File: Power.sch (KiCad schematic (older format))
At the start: 27 parts, among them J16 +15V, J17 GND, J18 WE 691216710002, J19 Conn_02x04_Counter_Clockwise, J20 Conn_02x04_Counter_Clockwise, J21 Conn_02x04_Counter_Clockwise, U8 AMS1117-3.3, U9 AMS1117-3.3

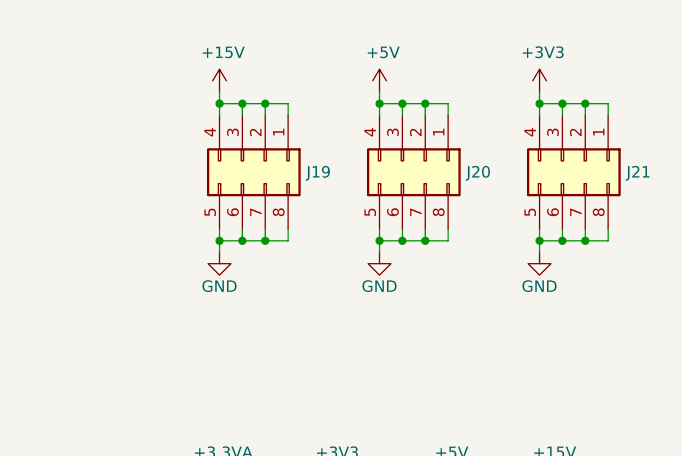
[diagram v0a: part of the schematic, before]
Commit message: MCU prepped for fanout
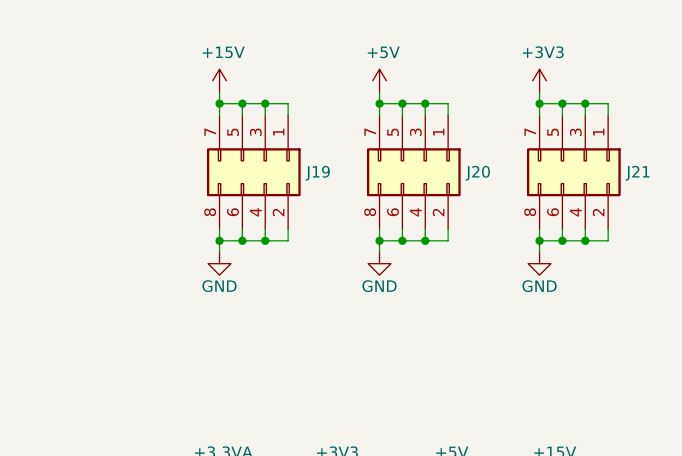
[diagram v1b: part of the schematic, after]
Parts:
- removed J19, J20, J21: Conn_02x04_Counter_Clockwise, Connector_PinHeader_2.54mm:PinHeader_2x04_P2.54mm_Vertical, symbol Connector_Generic:Conn_02x04_Counter_Clockwise
- added J19, J20, J21: Conn_02x04_Odd_Even, Connector_PinHeader_2.54mm:PinHeader_2x04_P2.54mm_Vertical, symbol Connector_Generic:Conn_02x04_Odd_Even
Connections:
- net +15V: now also J19.1 (Pin_1), J19.3 (Pin_3), J19.5 (Pin_5), J19.7 (Pin_7)
- net +3V3: now also J21.1 (Pin_1), J21.3 (Pin_3), J21.5 (Pin_5), J21.7 (Pin_7)
- net +5V: now also J20.1 (Pin_1), J20.3 (Pin_3), J20.5 (Pin_5), J20.7 (Pin_7)
- net GND: now also J19.2 (Pin_2), J19.4 (Pin_4), J19.6 (Pin_6), J19.8 (Pin_8), J20.2 (Pin_2), J20.4 (Pin_4), J20.6 (Pin_6), J20.8 (Pin_8), J21.2 (Pin_2), J21.4 (Pin_4), J21.6 (Pin_6), J21.8 (Pin_8)
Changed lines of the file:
@@
 	2050 3800 2150 3800
-$Comp
-L Connector_Generic:Conn_02x04_Counter_Clockwise J19
-U 1 1 5FB8C091
-P 8500 2750
-F 0 "J19" V 8550 2930 50  0000 L CNN
-F 1 "Conn_02x04_Counter_Clockwise" V 8595 2930 50  0001 L CNN
-F 2 "Connector_PinHeader_2.54mm:PinHeader_2x04_P2.54mm_Vertical" H 8500 2750 50  0001 C CNN
-F 3 "~" H 8500 2750 50  0001 C CNN
-	1    8500 2750
-	0    1    1    0
-$EndComp
 $Comp
 L Connector:Screw_Terminal_01x02 J18
@@
 $EndComp
 $Comp
-L Connector_Generic:Conn_02x04_Counter_Clockwise J20
-U 1 1 5FBAA479
-P 9200 2750
-F 0 "J20" V 9250 2930 50  0000 L CNN
-F 1 "Conn_02x04_Counter_Clockwise" V 9295 2930 50  0001 L CNN
-F 2 "Connector_PinHeader_2.54mm:PinHeader_2x04_P2.54mm_Vertical" H 9200 2750 50  0001 C CNN
-F 3 "~" H 9200 2750 50  0001 C CNN
-	1    9200 2750
-	0    1    1    0
-$EndComp
-$Comp
-L Connector_Generic:Conn_02x04_Counter_Clockwise J21
-U 1 1 5FBAB598
-P 9900 2750
-F 0 "J21" V 9950 2930 50  0000 L CNN
-F 1 "Conn_02x04_Counter_Clockwise" V 9995 2930 50  0001 L CNN
-F 2 "Connector_PinHeader_2.54mm:PinHeader_2x04_P2.54mm_Vertical" H 9900 2750 50  0001 C CNN
-F 3 "~" H 9900 2750 50  0001 C CNN
-	1    9900 2750
-	0    1    1    0
-$EndComp
-$Comp
 L power:+5V #PWR099
 U 1 1 5FBABD3B
@@
 	1    0    0    -1
 $EndComp
+$Comp
+L Connector_Generic:Conn_02x04_Odd_Even J20
+U 1 1 5FB27D5D
+P 9200 2750
+F 0 "J20" V 9250 2930 50  0000 L CNN
+F 1 "Conn_02x04_Odd_Even" V 9295 2930 50  0001 L CNN
+F 2 "Connector_PinHeader_2.54mm:PinHeader_2x04_P2.54mm_Vertical" H 9200 2750 50  0001 C CNN
+F 3 "~" H 9200 2750 50  0001 C CNN
+	1    9200 2750
+	0    1    1    0
+$EndComp
+$Comp
+L Connector_Generic:Conn_02x04_Odd_Even J21
+U 1 1 5FB2830E
+P 9900 2750
+F 0 "J21" V 9950 2930 50  0000 L CNN
+F 1 "Conn_02x04_Odd_Even" V 9995 2930 50  0001 L CNN
+F 2 "Connector_PinHeader_2.54mm:PinHeader_2x04_P2.54mm_Vertical" H 9900 2750 50  0001 C CNN
+F 3 "~" H 9900 2750 50  0001 C CNN
+	1    9900 2750
+	0    1    1    0
+$EndComp
+$Comp
+L Connector_Generic:Conn_02x04_Odd_Even J19
+U 1 1 5FB258DA
+P 8500 2750
+F 0 "J19" V 8550 2930 50  0000 L CNN
+F 1 "Conn_02x04_Odd_Even" V 8595 2930 50  0001 L CNN
+F 2 "Connector_PinHeader_2.54mm:PinHeader_2x04_P2.54mm_Vertical" H 8500 2750 50  0001 C CNN
+F 3 "~" H 8500 2750 50  0001 C CNN
+	1    8500 2750
+	0    1    1    0
+$EndComp
 $EndSCHEMATC
